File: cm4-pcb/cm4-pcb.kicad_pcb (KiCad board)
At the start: 2 copper layers, 140 x 70.5 mm, 39 parts, among them J1 Conn_01x02_Pin, J2 Conn_01x02_Pin, J3 USB1125-GF-B, J4 Conn_02x03_Odd_Even, J5 Conn_01x04, J6 J0011D21NL, J7 Conn_01x02, U1 Pfostenstecker_6_2x3, U2 Pfostenstecker_6_2x3, U5 SMD-PUSH-BTN

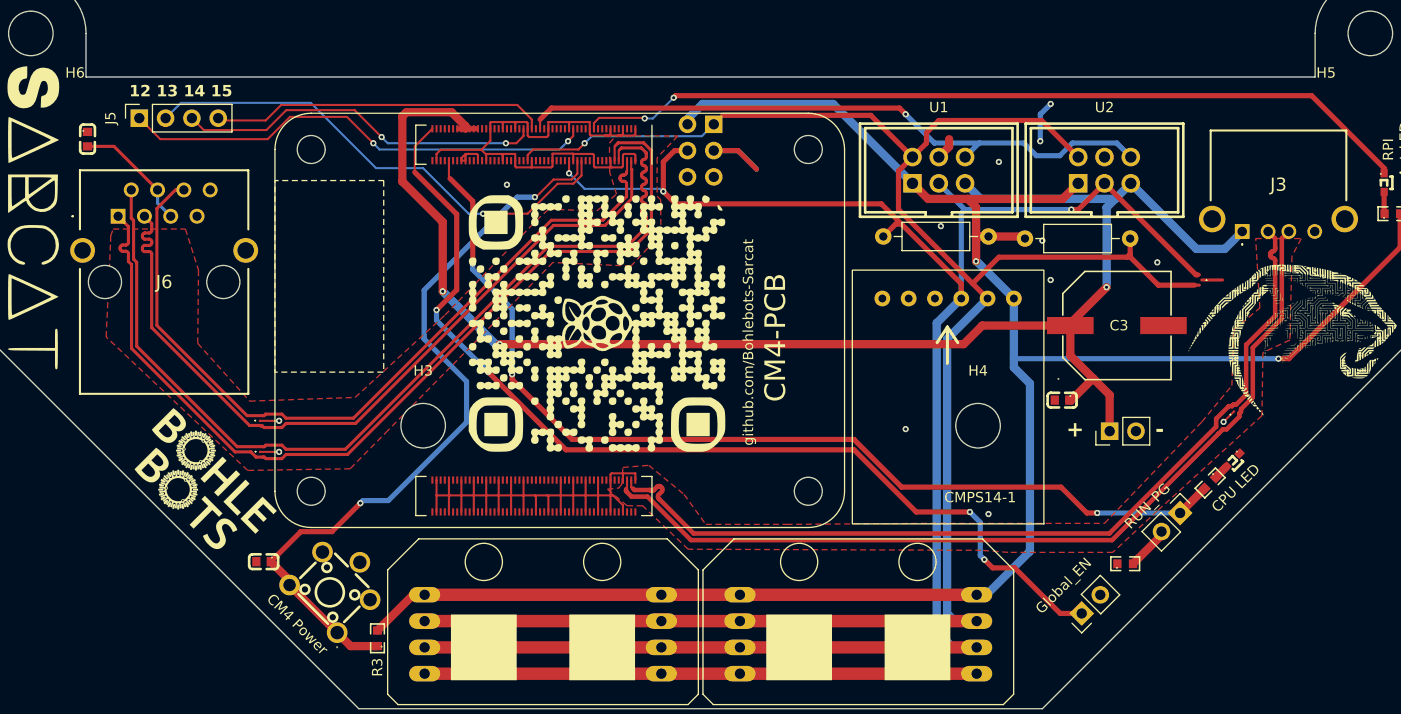
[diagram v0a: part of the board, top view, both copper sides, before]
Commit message: Added 5v Connector
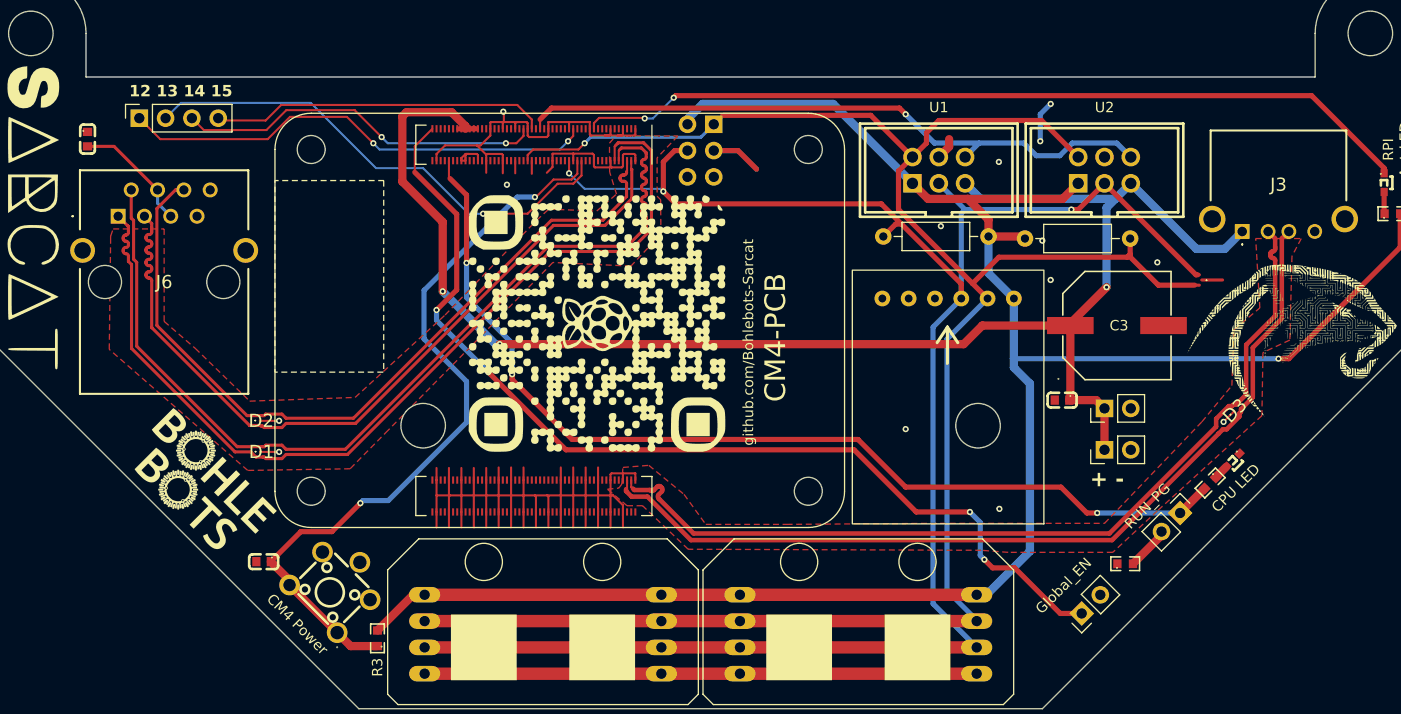
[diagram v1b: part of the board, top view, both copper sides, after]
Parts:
- added J8: Conn_01x02, Connector_PinHeader_2.54mm:PinHeader_1x02_P2.54mm_Vertical, F.Cu at (39.0, 67.0)
- moved J7 2.26 mm to (39.0, 63.0)
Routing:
- net GND: track 198.6 -> 236.7 mm, vias 13 -> 14
- net +3.3V: track 195.9 -> 194.5 mm, vias 2 -> 1
- net SDA: track 192.6 -> 191.4 mm
- net SCL: track 183.4 -> 182.3 mm
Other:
- board text added: "+ -"
- board text removed: "+"
- board text removed: "-"

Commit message: Fixed Traces
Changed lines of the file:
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@@
+	)
+	(segment
+		(start -14.403554 44.83)
+		(end -33.523554 63.95)
+		(width 0.3)
+		(layer "F.Cu")
+		(net 147)
 	)
 	(segment
@@
 	)
 	(segment
-		(start -42.149999 63.7)
-		(end -42.3 63.7)
+		(start -40.430761 63.55)
+		(end -41.999999 63.55)
+		(width 0.3)
+		(layer "F.Cu")
+		(net 147)
+	)
+	(segment
+		(start -40.030761 63.95)
+		(end -40.430761 63.55)
 		(width 0.3)
 		(layer "F.Cu")
@@
 		(start -43.792893 63.7)
 		(end -42.3 63.7)
+		(width 0.3)
+		(layer "F.Cu")
+		(net 147)
+	)
+	(segment
+		(start -7.251777 42.648223)
+		(end -9.433554 44.83)
+		(width 0.3)
+		(layer "F.Cu")
+		(net 147)
+	)
+	(segment
+		(start -7.15 42.298284)
+		(end -7.15 42.53)
 		(width 0.3)
 		(layer "F.Cu")
@@
 	)
 	(segment
+		(start -41.999999 63.55)
+		(end -42.149999 63.7)
+		(width 0.3)
+		(layer "F.Cu")
+		(net 147)
+	)
+	(segment
 		(start -9.433554 44.83)
 		(end -14.403554 44.83)
-		(width 0.3)
-		(layer "F.Cu")
-		(net 147)
-	)
-	(segment
-		(start -14.403554 44.83)
-		(end -33.523554 63.95)
-		(width 0.3)
-		(layer "F.Cu")
-		(net 147)
-	)
-	(segment
-		(start -7.15 42.466928)
-		(end -7.15 42.546446)
-		(width 0.3)
-		(layer "F.Cu")
-		(net 147)
-	)
-	(segment
-		(start -40.030761 63.95)
-		(end -40.430761 63.55)
-		(width 0.3)
-		(layer "F.Cu")
-		(net 147)
-	)
-	(segment
-		(start -7.15 41.31)
-		(end -7.15 41.43)
 		(width 0.3)
 		(layer "F.Cu")
@@
 	)
 	(segment
-		(start -7.15 40.13)
-		(end -7.15 40.23)
+		(start -7.15 41.098284)
+		(end -7.15 41.33)
 		(width 0.3)
 		(layer "F.Cu")
@@
 	(segment
 		(start -7.15 42.546446)
-		(end -9.433554 44.83)
-		(width 0.3)
-		(layer "F.Cu")
-		(net 147)
-	)
-	(segment
-		(start -7.536436 41.07)
-		(end -7.39 41.07)
-		(width 0.3)
-		(layer "F.Cu")
-		(net 147)
-	)
-	(segment
-		(start -7.15 41.43)
-		(end -7.15 42.466928)
-		(width 0.3)
-		(layer "F.Cu")
-		(net 147)
-	)
-	(segment
-		(start -7.776436 40.71)
-		(end -7.776436 40.83)
-		(width 0.3)
-		(layer "F.Cu")
-		(net 147)
-	)
-	(segment
-		(start -41.999999 63.55)
-		(end -42.149999 63.7)
+		(end -7.251777 42.648223)
+		(width 0.3)
+		(layer "F.Cu")
+		(net 147)
+	)
+	(segment
+		(start -42.149999 63.7)
+		(end -42.3 63.7)
+		(width 0.3)
+		(layer "F.Cu")
+		(net 147)
+	)
+	(segment
+		(start -7.15 42.53)
+		(end -7.15 42.546446)
+		(width 0.3)
+		(layer "F.Cu")
+		(net 147)
+	)
+	(segment
+		(start -7.518284 41.698284)
+		(end -7.518284 41.93)
 		(width 0.3)
 		(layer "F.Cu")
@@
 	)
 	(segment
-		(start -7.39 40.47)
-		(end -7.536436 40.47)
-		(width 0.3)
-		(layer "F.Cu")
-		(net 147)
-	)
-	(segment
-		(start -40.430761 63.55)
-		(end -41.999999 63.55)
-		(width 0.3)
-		(layer "F.Cu")
-		(net 147)
-	)
-	(arc
-		(start -7.15 40.23)
-		(mid -7.220294 40.399706)
-		(end -7.39 40.47)
-		(width 0.3)
-		(layer "F.Cu")
-		(net 147)
-	)
-	(arc
-		(start -7.776436 40.83)
-		(mid -7.706142 40.999706)
-		(end -7.536436 41.07)
-		(width 0.3)
-		(layer "F.Cu")
-		(net 147)
-	)
-	(arc
-		(start -7.536436 40.47)
-		(mid -7.706142 40.540294)
-		(end -7.776436 40.71)
-		(width 0.3)
-		(layer "F.Cu")
-		(net 147)
-	)
-	(arc
-		(start -7.39 41.07)
-		(mid -7.220294 41.140294)
-		(end -7.15 41.31)
+		(start -7.518284 40.498284)
+		(end -7.518284 40.73)
+		(width 0.3)
+		(layer "F.Cu")
+		(net 147)
+	)
+	(arc
+		(start -7.518284 41.93)
+		(mid -7.46435 42.060208)
+		(end -7.334142 42.114142)
+		(width 0.3)
+		(layer "F.Cu")
+		(net 147)
+	)
+	(arc
+		(start -7.15 41.33)
+		(mid -7.203934 41.460208)
+		(end -7.334142 41.514142)
+		(width 0.3)
+		(layer "F.Cu")
+		(net 147)
+	)
+	(arc
+		(start -7.334142 40.314142)
+		(mid -7.46435 40.368076)
+		(end -7.518284 40.498284)
+		(width 0.3)
+		(layer "F.Cu")
+		(net 147)
+	)
+	(arc
+		(start -7.518284 40.73)
+		(mid -7.46435 40.860208)
+		(end -7.334142 40.914142)
+		(width 0.3)
+		(layer "F.Cu")
+		(net 147)
+	)
+	(arc
+		(start -7.15 40.13)
+		(mid -7.203934 40.260208)
+		(end -7.334142 40.314142)
+		(width 0.3)
+		(layer "F.Cu")
+		(net 147)
+	)
+	(arc
+		(start -7.334142 40.914142)
+		(mid -7.203934 40.968076)
+		(end -7.15 41.098284)
+		(width 0.3)
+		(layer "F.Cu")
+		(net 147)
+	)
+	(arc
+		(start -7.334142 42.114142)
+		(mid -7.203934 42.168076)
+		(end -7.15 42.298284)
+		(width 0.3)
+		(layer "F.Cu")
+		(net 147)
+	)
+	(arc
+		(start -7.334142 41.514142)
+		(mid -7.46435 41.568076)
+		(end -7.518284 41.698284)
 		(width 0.3)
 		(layer "F.Cu")
@@
 		(base_line
 			(pts
-				(xy -7.15 40.23) (xy -7.15 42.466928)
+				(xy -7.15 40.13) (xy -7.15 42.546446) (xy -7.251777 42.648223)
 			)
 		)
@@
 		(corner_radius_percent 80)
 		(end
-			(xy -7.15 42.466928)
+			(xy -7.251777 42.648223)
 		)
 		(initial_side "right")
@@
 		(last_status "tuned")
 		(last_track_width 0.3)
-		(last_tuning "-0.0000 mm (tuned)")
-		(max_amplitude 1)
-		(min_amplitude 0.2)
-		(min_spacing 0.6)
-		(origin
-			(xy -7.15 40.23)
-		)
-		(override_custom_rules no)
-		(rounded yes)
-		(single_sided no)
-		(target_length 1000000)
-		(target_length_max 1000000.1)
-		(target_length_min 999999.9)
-		(target_skew 0)
-		(target_skew_max 0.1)
-		(target_skew_min -0.1)
+		(last_tuning "0.0000 mm (tuned)")
+		(max_amplitude 0.5)
+		(min_amplitude 0.2)
+		(min_spacing 0.6)
+		(origin
+			(xy -7.15 40.13)
+		)
+		(override_custom_rules no)
+		(rounded yes)
+		(single_sided no)
+		(target_length 1000000)
+		(target_length_max 1000000.1)
+		(target_length_min 999999.9)
+		(target_skew 0)
+		(target_skew_max 2147.483647)
+		(target_skew_min 0)
 		(tuning_mode "diff_pair_skew")
-		(members 1ba4a44c-5792-418e-b643-f8bec25f70e1 27e45d77-f731-43af-bf41-c23da0fbe238
-			3c629bd7-93b4-4f83-a25a-b3ab71092ccd 778c99dd-435a-40c8-96e0-bca0f1753657
-			a833130c-2d9c-4db1-928f-bbee91bff4a1 abd2e56e-b74e-4e18-bcf0-572e6cfbf027
-			ad7279be-f590-4181-aa95-79a6dce7a586 af2e2c63-0cec-4fe2-b946-5b59075b80be
-			d20978b7-7a76-43ea-92f7-deeab731905c
-		)
-	)
+		(members 08a0ce4c-9dbc-4067-a3a8-e87b9943b050 0fbdda6b-9871-4887-ac59-faa765e28b09
+			26891050-744d-40c2-988f-f928f1099077 2ca990a3-f7de-4ff0-bb89-897f4985fd05
+			505e0869-8fce-4688-88d1-749a16daba8f 5ef70eba-6205-4892-a705-c3ee30d58f46
+			88759b40-306f-4350-ad8d-d5de821055f3 9c8cc4d3-921c-48df-9d25-0044d1b89147
+			a4080fca-5fd8-44bc-ba4a-9e9ebedc513a b4f3dd1a-36b6-4e1e-b17b-c1e749076057
+			b711bfdf-408a-4af0-a15d-c2c2e741c3a0 c008754b-e79e-4e01-afbb-381e3f3eccd0
+			e1852efe-1e38-452c-9ea7-e0eb93a3e542 eb84f41c-5159-4833-b9ef-d69b4dc8d6f5
+		)
+	)

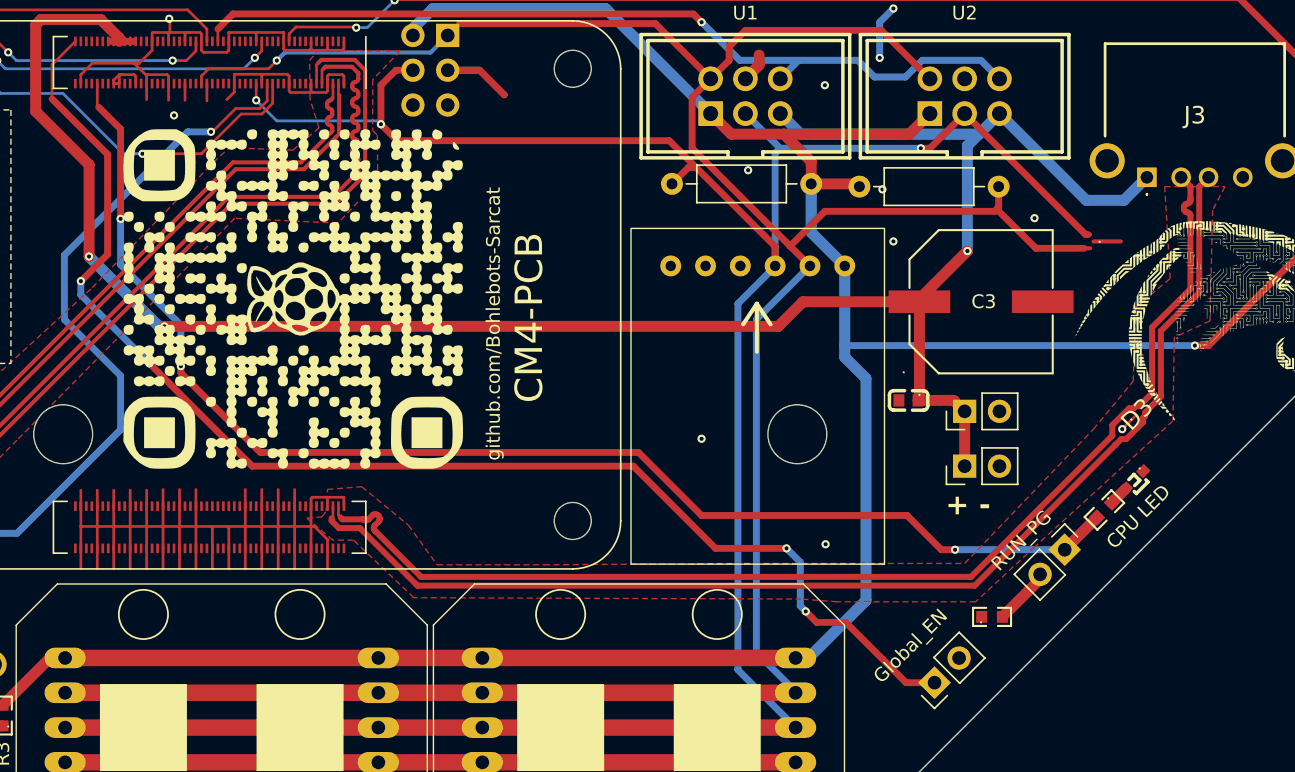
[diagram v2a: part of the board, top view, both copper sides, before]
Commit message: Pins Analog Input
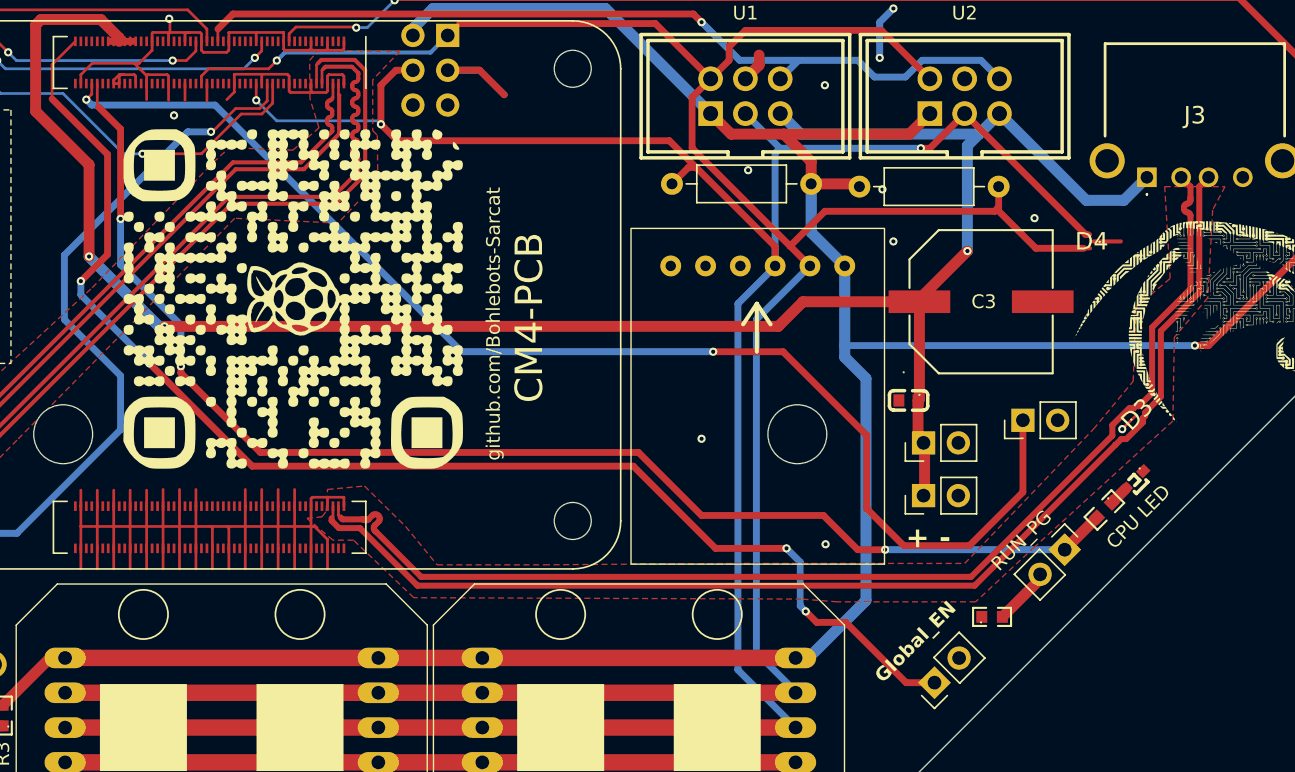
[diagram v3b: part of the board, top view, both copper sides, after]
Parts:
- added J9: Conn_01x02_Pin, Connector_PinHeader_2.54mm:PinHeader_1x02_P2.54mm_Vertical, F.Cu at (43.2, 63.6)
- moved J7 3.78 mm to (36.0, 65.3)
- moved J8 3.69 mm to (36.0, 69.2)
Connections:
- Module1 pad 94: unconnected-(Module1A-AnalogIP1-Pad94) -> A1
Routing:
- net A1: track 0.00 -> 93.2 mm, vias 0 -> 2
- net +5V: track 151.1 -> 150.5 mm
